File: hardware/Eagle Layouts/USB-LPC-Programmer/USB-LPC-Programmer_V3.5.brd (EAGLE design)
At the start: 71.9 x 25.9 mm, 22 parts, among them IC1 FT232RL, IC2 74HCT02N, Q1 ASE 7,3728MHz, Q2 7,3728MHz, T1 BC557, X1 USB BW

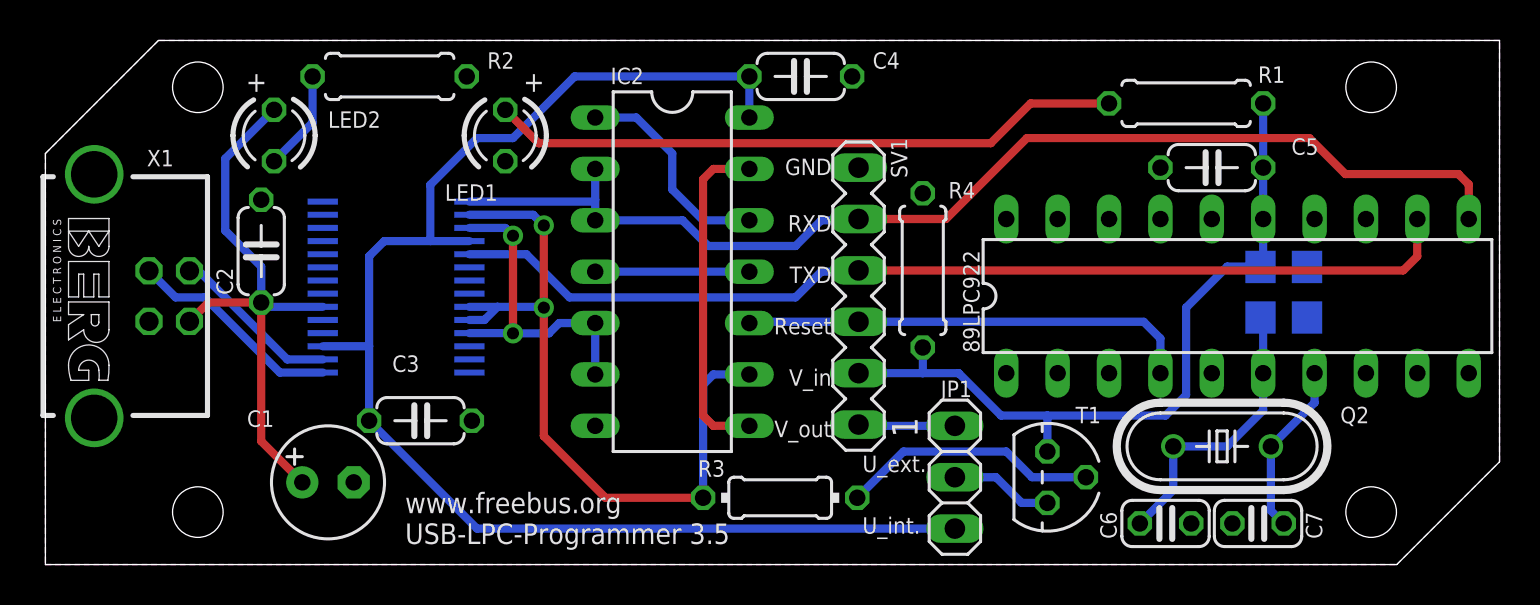
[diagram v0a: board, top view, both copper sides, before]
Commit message: Beschreibung ergänzt, Quarzposition korrigiert
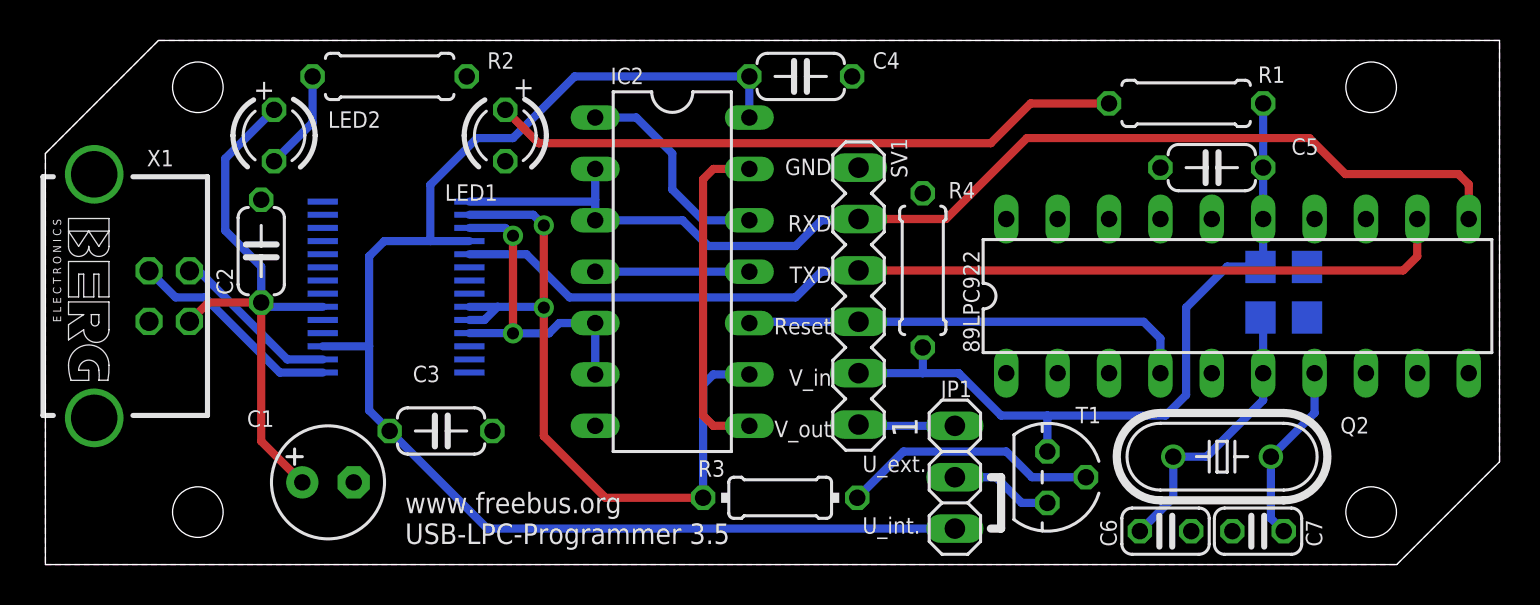
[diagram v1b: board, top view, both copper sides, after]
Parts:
- moved C3 1.14 mm to (19.6, 6.60)
- moved Q2 0.51 mm to (58.2, 5.33)
- moved C6 0.38 mm to (55.4, 1.65)
- moved C7 0.38 mm to (59.9, 1.65)
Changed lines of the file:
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@@
 <setting verticaltext="up"/>
 </settings>
-<grid distance="0.01" unitdist="inch" unit="mm" style="lines" multiple="1" display="yes" altdistance="0" altunitdist="inch" altunit="inch"/>
+<grid distance="0.01" unitdist="inch" unit="inch" style="lines" multiple="1" display="yes" altdistance="0.005" altunitdist="inch" altunit="inch"/>
 <layers>
 <layer number="1" name="Top" color="4" fill="1" visible="yes" active="yes"/>
@@
 <text x="38.862" y="17.272" size="0.8128" layer="21" rot="R180">RXD</text>
 <text x="38.862" y="20.066" size="0.8128" layer="21" rot="R180">GND</text>
-<text x="9.906" y="23.368" size="1.016" layer="21">+</text>
-<text x="23.622" y="23.368" size="1.016" layer="21">+</text>
+<text x="10.287" y="22.987" size="1.016" layer="21">+</text>
+<text x="23.114" y="23.114" size="1.016" layer="21">+</text>
+<wire x1="46.736" y1="4.318" x2="47.244" y2="4.318" width="0.4064" layer="21"/>
+<wire x1="47.244" y1="4.318" x2="47.244" y2="1.778" width="0.4064" layer="21"/>
+<wire x1="47.244" y1="1.778" x2="46.736" y2="1.778" width="0.4064" layer="21"/>
 </plain>
 <attributes>
@@
 <attribute name="VALUE" x="12.827" y="13.335" size="0.8128" layer="27" ratio="10" rot="R90"/>
 </element>
-<element name="C3" library="rcl" package="C050-024X044" value="100nF" x="18.542" y="7.112" smashed="yes">
-<attribute name="NAME" x="17.145" y="9.525" size="0.8128" layer="25" ratio="10"/>
-<attribute name="VALUE" x="17.145" y="8.509" size="0.8128" layer="27" ratio="10"/>
+<element name="C3" library="rcl" package="C050-024X044" value="100nF" x="19.558" y="6.604" smashed="yes">
+<attribute name="NAME" x="18.161" y="9.017" size="0.8128" layer="25" ratio="10"/>
+<attribute name="VALUE" x="18.161" y="8.001" size="0.8128" layer="27" ratio="10"/>
 </element>
 <element name="IC1" library="ftdi4" package="SSOP-28" value="FT232RL" x="17.3355" y="13.716" smashed="yes" rot="MR270">
@@
 <attribute name="VALUE" x="14.986" y="23.8252" size="0.8128" layer="27" ratio="10"/>
 </element>
-<element name="Q2" library="crystal" package="HC49/S" value="7,3728MHz" x="58.166" y="5.842" smashed="yes" rot="R180">
-<attribute name="NAME" x="64.008" y="6.985" size="0.8128" layer="25" ratio="10"/>
-<attribute name="VALUE" x="64.008" y="5.969" size="0.8128" layer="27" ratio="10"/>
-<attribute name="OC_NEWARK" value="unknown" x="58.166" y="5.842" size="1.778" layer="27" rot="R180" display="off"/>
-<attribute name="MPN" value="" x="58.166" y="5.842" size="1.778" layer="27" rot="R180" display="off"/>
-<attribute name="MF" value="" x="58.166" y="5.842" size="1.778" layer="27" rot="R180" display="off"/>
-<attribute name="OC_FARNELL" value="1667008" x="58.166" y="5.842" size="1.778" layer="27" rot="R180" display="off"/>
-</element>
-<element name="C7" library="rcl" package="C025-024X044" value="33p" x="59.944" y="2.032" smashed="yes" rot="R180">
-<attribute name="NAME" x="63.119" y="1.27" size="0.8128" layer="25" ratio="10" rot="R90"/>
-</element>
-<element name="C6" library="rcl" package="C025-024X044" value="33p" x="55.372" y="2.032" smashed="yes">
-<attribute name="NAME" x="52.959" y="1.27" size="0.8128" layer="25" ratio="10" rot="R90"/>
+<element name="Q2" library="crystal" package="HC49/S" value="7,3728MHz" x="58.166" y="5.334" smashed="yes" rot="R180">
+<attribute name="NAME" x="64.008" y="6.477" size="0.8128" layer="25" ratio="10"/>
+<attribute name="VALUE" x="64.008" y="5.461" size="0.8128" layer="27" ratio="10"/>
+<attribute name="OC_NEWARK" value="unknown" x="58.166" y="5.334" size="1.778" layer="27" rot="R180" display="off"/>
+<attribute name="MPN" value="" x="58.166" y="5.334" size="1.778" layer="27" rot="R180" display="off"/>
+<attribute name="MF" value="" x="58.166" y="5.334" size="1.778" layer="27" rot="R180" display="off"/>
+<attribute name="OC_FARNELL" value="1667008" x="58.166" y="5.334" size="1.778" layer="27" rot="R180" display="off"/>
+</element>
+<element name="C7" library="rcl" package="C025-024X044" value="33p" x="59.944" y="1.651" smashed="yes" rot="R180">
+<attribute name="NAME" x="63.119" y="0.889" size="0.8128" layer="25" ratio="10" rot="R90"/>
+</element>
+<element name="C6" library="rcl" package="C025-024X044" value="33p" x="55.372" y="1.651" smashed="yes">
+<attribute name="NAME" x="52.959" y="0.889" size="0.8128" layer="25" ratio="10" rot="R90"/>
 </element>
 <element name="C5" library="rcl" package="C050-024X044" value="100nF" x="57.658" y="19.6215" smashed="yes">
@@
 <wire x1="23.114" y1="21.082" x2="26.162" y2="24.13" width="0.4064" layer="16"/>
 <wire x1="26.162" y1="24.13" x2="34.798" y2="24.13" width="0.4064" layer="16"/>
-<wire x1="16.002" y1="10.791" x2="16.002" y2="7.112" width="0.4064" layer="16"/>
-<wire x1="16.002" y1="7.112" x2="21.336" y2="1.778" width="0.4064" layer="16"/>
-<wire x1="21.336" y1="1.778" x2="44.958" y2="1.778" width="0.4064" layer="16"/>
+<wire x1="16.002" y1="10.791" x2="16.002" y2="7.62" width="0.4064" layer="16"/>
+<wire x1="16.002" y1="7.62" x2="17.018" y2="6.604" width="0.4064" layer="16"/>
+<wire x1="44.958" y1="1.778" x2="21.844" y2="1.778" width="0.4064" layer="16"/>
+<wire x1="21.844" y1="1.778" x2="17.018" y2="6.604" width="0.4064" layer="16"/>
 </signal>
 <signal name="N$9">
@@
 <contactref element="Q1" pad="3"/>
 <contactref element="89LPC922" pad="6"/>
-<wire x1="55.753" y1="5.842" x2="58.42" y2="5.842" width="0.4064" layer="16"/>
-<wire x1="58.42" y1="5.842" x2="60.198" y2="7.62" width="0.4064" layer="16"/>
-<wire x1="60.198" y1="7.62" x2="60.198" y2="9.4615" width="0.4064" layer="16"/>
 <wire x1="60.198" y1="9.4615" x2="60.198" y2="12.212" width="0.4064" layer="16"/>
 <wire x1="60.198" y1="12.212" x2="60.064" y2="12.212" width="0.4064" layer="16"/>
-<wire x1="55.753" y1="5.842" x2="55.753" y2="3.683" width="0.4064" layer="16"/>
-<wire x1="55.753" y1="3.683" x2="54.102" y2="2.032" width="0.4064" layer="16"/>
+<wire x1="60.198" y1="9.4615" x2="60.198" y2="8.128" width="0.4064" layer="16"/>
+<wire x1="60.198" y1="8.128" x2="57.404" y2="5.334" width="0.4064" layer="16"/>
+<wire x1="57.404" y1="5.334" x2="55.753" y2="5.334" width="0.4064" layer="16"/>
+<wire x1="55.753" y1="5.334" x2="55.753" y2="3.302" width="0.4064" layer="16"/>
+<wire x1="55.753" y1="3.302" x2="54.102" y2="1.651" width="0.4064" layer="16"/>
 </signal>
 <signal name="XTAL2">
@@
 <contactref element="Q2" pad="1"/>
 <contactref element="89LPC922" pad="7"/>
-<wire x1="62.738" y1="9.4615" x2="62.738" y2="8.001" width="0.4064" layer="16"/>
-<wire x1="62.738" y1="8.001" x2="60.579" y2="5.842" width="0.4064" layer="16"/>
-<wire x1="60.579" y1="5.842" x2="60.579" y2="2.667" width="0.4064" layer="16"/>
-<wire x1="60.579" y1="2.667" x2="61.214" y2="2.032" width="0.4064" layer="16"/>
+<wire x1="62.738" y1="9.4615" x2="62.738" y2="7.493" width="0.4064" layer="16"/>
+<wire x1="62.738" y1="7.493" x2="60.579" y2="5.334" width="0.4064" layer="16"/>
+<wire x1="60.579" y1="5.334" x2="60.579" y2="2.286" width="0.4064" layer="16"/>
+<wire x1="60.579" y1="2.286" x2="61.214" y2="1.651" width="0.4064" layer="16"/>
 </signal>
 </signals>
